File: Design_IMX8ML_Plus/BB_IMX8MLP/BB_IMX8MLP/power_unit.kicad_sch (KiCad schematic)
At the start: 0 parts

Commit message: Improve power source module in the base board
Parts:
- added C10, C12, C26, C27, C4, C7, C8: 100nF, Capacitor_SMD:C_0402_1005Metric, symbol Device:C_Small
- added C11, C14, C15, C16, C20, C5, C6: 10uF, Capacitor_SMD:C_0402_1005Metric, symbol Device:C_Small
- added C13: 1uF, Capacitor_SMD:C_0402_1005Metric, symbol Device:C_Small
- added C17, C18, C19, C21, C22, C23, C24, C3: 47uF, Capacitor_SMD:C_0402_1005Metric, symbol Device:C_Small
- added C25, C9: 4.7uF, Capacitor_SMD:C_0402_1005Metric, symbol Device:C_Small
- added D1: SS3200, Diode_SMD:D_SMA, symbol Diode:SS3200
- added F1: 10A 36R@100MHz, Fuse:Fuse_0603_1608Metric, symbol Device:Fuse_Small
- added J10: Barrel_Jack, Connector_BarrelJack:BarrelJack_CUI_PJ-063AH_Horizontal, symbol Connector:Barrel_Jack
- added L1, L2: 2.2uH_12A, Inductor_SMD:L_7.3x7.3_H3.5, symbol Device:L_Small
- added Q1, Q4: PMDT290UCE, Package_TO_SOT_SMD:SOT-666, symbol Transistor_FET:PMDT290UCE
- added Q2, Q3: NTMFS5C670NLT1G, _W_SBC:NTMFS5C670NLT1G_ONS, symbol NTMFS5C670NLT1G:NTMFS5C670NLT1G
- added R1, R19: 47K, Resistor_SMD:R_0402_1005Metric, symbol Device:R_Small
- added R10, R16, R17, R18, R21, R23, R3, R4, R5, R7, R8, R9: 100K, Resistor_SMD:R_0402_1005Metric, symbol Device:R_Small
- added R11: 787K, Resistor_SMD:R_0402_1005Metric, symbol Device:R_Small
- added R12, R14: 80.6K, Resistor_SMD:R_0402_1005Metric, symbol Device:R_Small
- added R13: 18.2K, Resistor_SMD:R_0402_1005Metric, symbol Device:R_Small
- added R15: 0.01, Resistor_SMD:R_0402_1005Metric, symbol Device:R_Small
- added R2, R20: 8.87K, Resistor_SMD:R_0402_1005Metric, symbol Device:R_Small
- added R22, R6: 510K, Resistor_SMD:R_0402_1005Metric, symbol Device:R_Small
- added SW1: Power ON/OFF, Button_Switch_SMD:SW_SPST_TL3342, symbol Switch:SW_MEC_5E
- added SW2: RESET, Button_Switch_SMD:SW_SPST_TL3342, symbol Switch:SW_MEC_5E
- added SW3: RECOVERY, Button_Switch_SMD:SW_SPST_TL3342, symbol Switch:SW_MEC_5E
- added U4: LTC4368IDD-1_PBF, Package_DFN_QFN:DFN-10-1EP_3x3mm_P0.5mm_EP1.65x2.38mm, symbol LTC4368IDD-1_PBF:LTC4368IDD-1_PBF
- added U5, U7: AOZ2261AQI-15, _W_SBC:QFN4X4-22L_EP2_S_AOS, symbol AOZ2261AQI-15:AOZ2261AQI-15
- added U6: NCV4274CST50T3G, Package_TO_SOT_SMD:SOT-223, symbol NCV4274CST50T3G:NCV4274CST50T3G
- added U8: LTC2954CDDB-1-TRMPBF, _W_SBC:DFN-8_DDB_LIT, symbol LTC2954CDDB-2:LTC2954CDDB-1-TRMPBF
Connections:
- new net: R4.1, U5.3 (*PFM)
- new net: C13.1, U8.6 (PDT)
- new net: SW1.3 (K), SW1.4 (A), U8.3 (*PB)
- new net: R7.1, U8.5 (*KILL)
- new net: R3.2, U5.1 (PGOOD)
- new net: C5.1, R14.2
- new net: R12.2, R13.1, U4.3 (OV)
- new net: C8.1, U5.22 (SS)
- new net: Q4.3 (DP), R18.1, U7.2 (EN)
- new net: C27.1, U7.22 (SS)
- new net: R21.1, U7.3 (*PFM)
- new net: R22.2, U7.6 (TON)
- new net: C7.2, L1.2, U5.10 (LX), U5.11 (LX), U5.16 (LX), U5.17 (LX), U5.18 (LX)
- new net: C7.1, U5.20 (BST)
- new net: C4.1, U4.4 (RETRY)
- new net: C6.1, D1.1 (K), F1.1, J10.1
- new net: C20.1, F1.2, Q3.5, Q3.6, R10.1, U4.1 (VIN)
- new net: Q4.5 (GP), R16.2, R17.2
- new net: Q1.5 (GP), R8.2, R9.2
- new net: Q2.4, Q3.4, R14.1, U4.10 (GATE)
- new net: R11.2, R12.1, U4.2 (UV)
- new net: R10.2, R11.1, U4.6 (~{SHDN})
- new net: Q2.5, Q2.6, R15.1, U4.8 (VOUT), U4.9 (SENSE)
- new net: R6.2, U5.6 (TON)
- new net: Q1.3 (DP), R5.1, U5.2 (EN)
- new net: R23.2, U7.1 (PGOOD)
- new net: C26.2, L2.2, U7.10 (LX), U7.11 (LX), U7.16 (LX), U7.17 (LX), U7.18 (LX)
- new net: C26.1, U7.20 (BST)
- new net: Q2.1, Q2.2, Q2.3, Q3.1, Q3.2, Q3.3
- new net: SW2.3 (K), SW2.4 (A)
- new net: SW3.3 (K), SW3.4 (A)
- new net +5V: C17.1, C18.1, C19.1, C21.1, C22.1, C23.1, C24.1, C3.1, L1.1, L2.1, R1.1, R19.1
- new net +V5_STB: C11.1, C12.1, Q1.4 (SP), Q4.4 (SP), R17.1, R7.2, R8.1, U6.3 (Q), U8.4 (VIN)
- new net +V_STB: C25.1, C9.1, R23.1, R3.1, U5.21 (VCC), U7.21 (VCC)
- new net +V_SUPPLY_FILT: C10.1, C14.1, C15.1, C16.1, R15.2, R22.1, R6.1, U5.7 (IN), U5.8 (IN), U5.9 (IN), U6.1 (I), U7.7 (IN), U7.8 (IN), U7.9 (IN)
- new net 5V_EN: R16.1, R9.1, U8.7 (EN/*EN)
- new net FB_5V: R1.2, R19.2, R2.1, R20.1, U5.5 (FB), U7.5 (FB)
- new net GND: C10.2, C11.2, C12.2, C13.2, C14.2, C15.2, C16.2, C17.2, C18.2, C19.2, C20.2, C21.2, C22.2, C23.2, C24.2, C25.2, C27.2, C3.2, C4.2, C5.2, C6.2, C8.2, C9.2, D1.2 (A), J10.2, R13.2, R18.2, R2.2, R20.2, R21.2, R4.2, R5.2, SW1.1, SW1.2, SW2.1, SW2.2, SW3.1, SW3.2, U4.11 (EXP), U4.5 (GND), U5.12 (PGND), U5.13 (PGND), U5.14 (PGND), U5.15 (PGND), U5.19 (PGND), U5.4 (AGND), U6.2 (GND), U6.4 (GND), U7.12 (PGND), U7.13 (PGND), U7.14 (PGND), U7.15 (PGND), U7.19 (PGND), U7.4 (AGND), U8.1 (GND), U8.9 (EPAD)
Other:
- company: (none) -> William Sanchez Farfan
- title: (none) -> Base board desgin

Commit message: improving the usb conector
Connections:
- net +V5_STB: now also U8.3 (*PB)
- net CTRL_ON/OFF: now reaches SW1.3 (K), SW1.4 (A)
- net CTRL_ON/OFF: no longer U8.3 (*PB)
- net CTRL_RESET: now reaches SW2.3 (K), SW2.4 (A)
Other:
- moved on the sheet: C12, C13, R7, SW1, SW2, SW3, U8

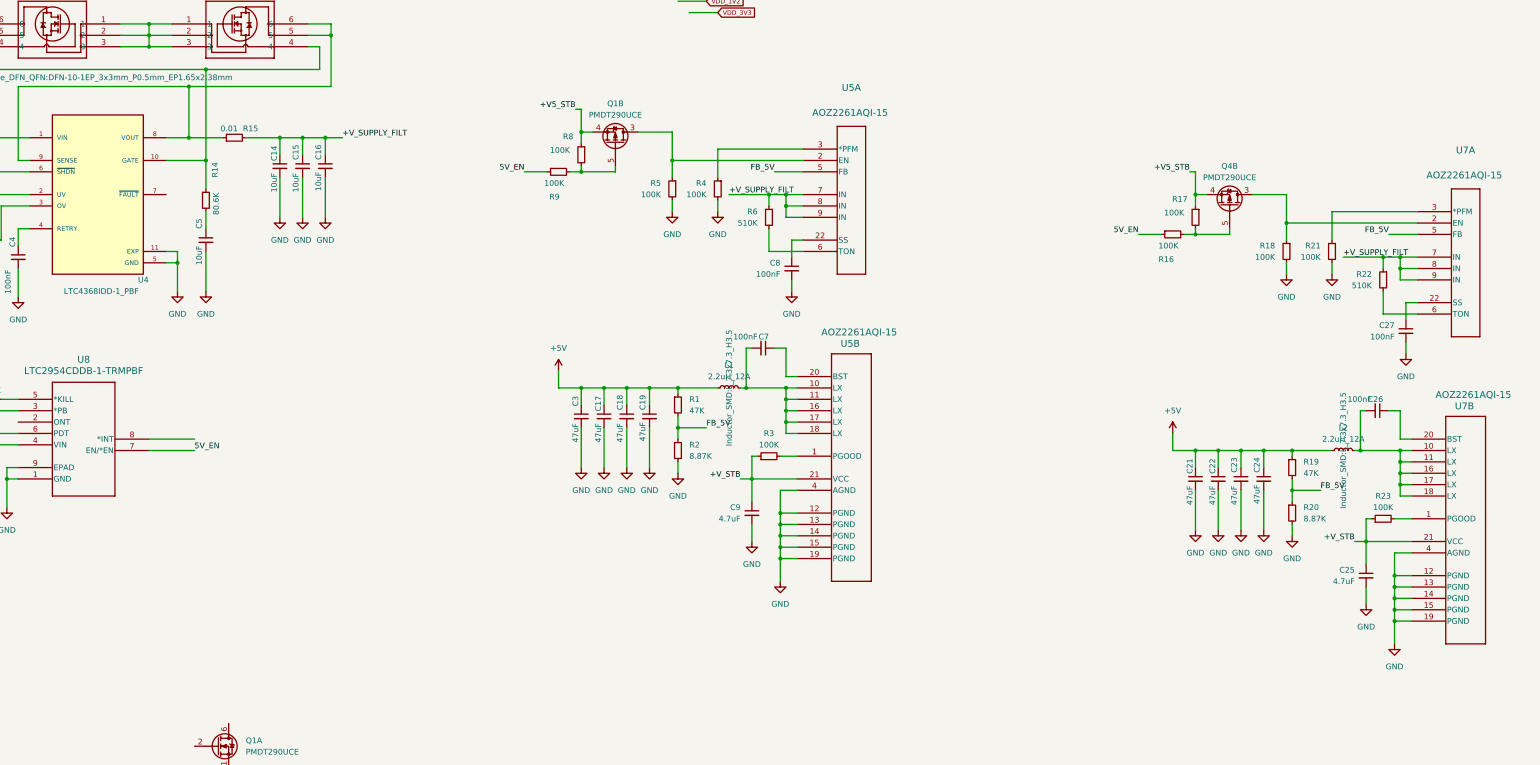
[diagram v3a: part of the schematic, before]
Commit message: improving Ethernet, USB and Camera inteface
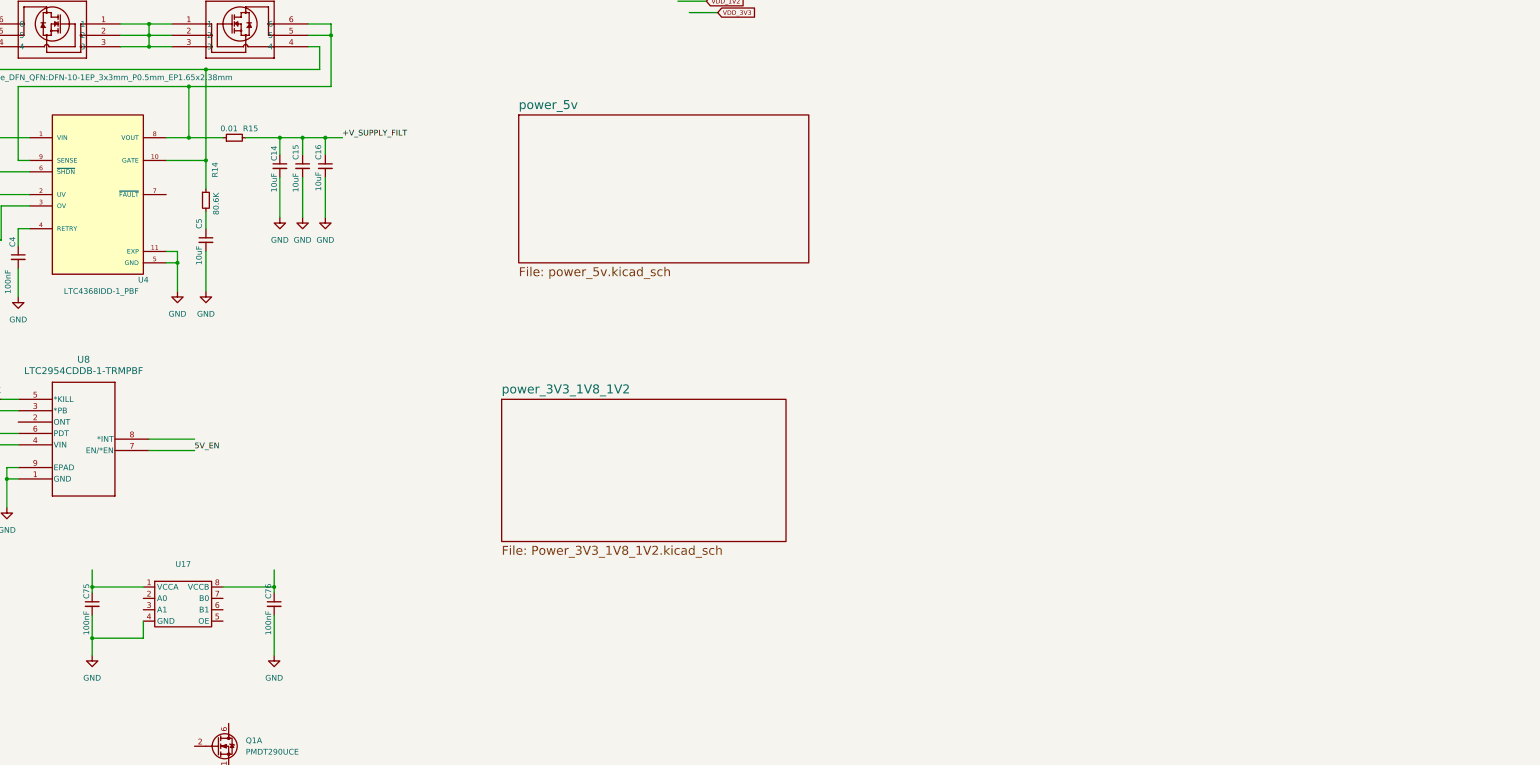
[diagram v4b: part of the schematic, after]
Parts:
- removed C17, C18, C19, C21, C22, C23, C24, C3: 47uF, Capacitor_SMD:C_0402_1005Metric, symbol Device:C_Small
- removed C25, C9: 4.7uF, Capacitor_SMD:C_0402_1005Metric, symbol Device:C_Small
- removed C26, C27, C7, C8: 100nF, Capacitor_SMD:C_0402_1005Metric, symbol Device:C_Small
- removed L1, L2: 2.2uH_12A, Inductor_SMD:L_7.3x7.3_H3.5, symbol Device:L_Small
- removed unit 2 of Q1
- removed Q4: PMDT290UCE, Package_TO_SOT_SMD:SOT-666, symbol Transistor_FET:PMDT290UCE
- removed R1, R19: 47K, Resistor_SMD:R_0402_1005Metric, symbol Device:R_Small
- removed R16, R17, R18, R21, R23, R3, R4, R5, R8, R9: 100K, Resistor_SMD:R_0402_1005Metric, symbol Device:R_Small
- removed R2, R20: 8.87K, Resistor_SMD:R_0402_1005Metric, symbol Device:R_Small
- removed R22, R6: 510K, Resistor_SMD:R_0402_1005Metric, symbol Device:R_Small
- removed U5, U7: AOZ2261AQI-15, _W_SBC:QFN4X4-22L_EP2_S_AOS, symbol AOZ2261AQI-15:AOZ2261AQI-15
- added C75, C76: 100nF, Capacitor_SMD:C_0402_1005Metric, symbol Device:C_Small
- added U17: ~, _W_SBC:MICROPAK8_1P6X1P6_ONS, symbol _W_MX8M:FXMA2102L8X
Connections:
- net GND: now also C75.2, C76.2, U17.4 (GND)
- new net: C75.1, U17.1 (VCCA)
- new net: C76.1, U17.8 (VCCB)
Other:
- added sheet power_3V3_1V8_1V2 (Power_3V3_1V8_1V2.kicad_sch)
- added sheet power_5v (power_5v.kicad_sch)

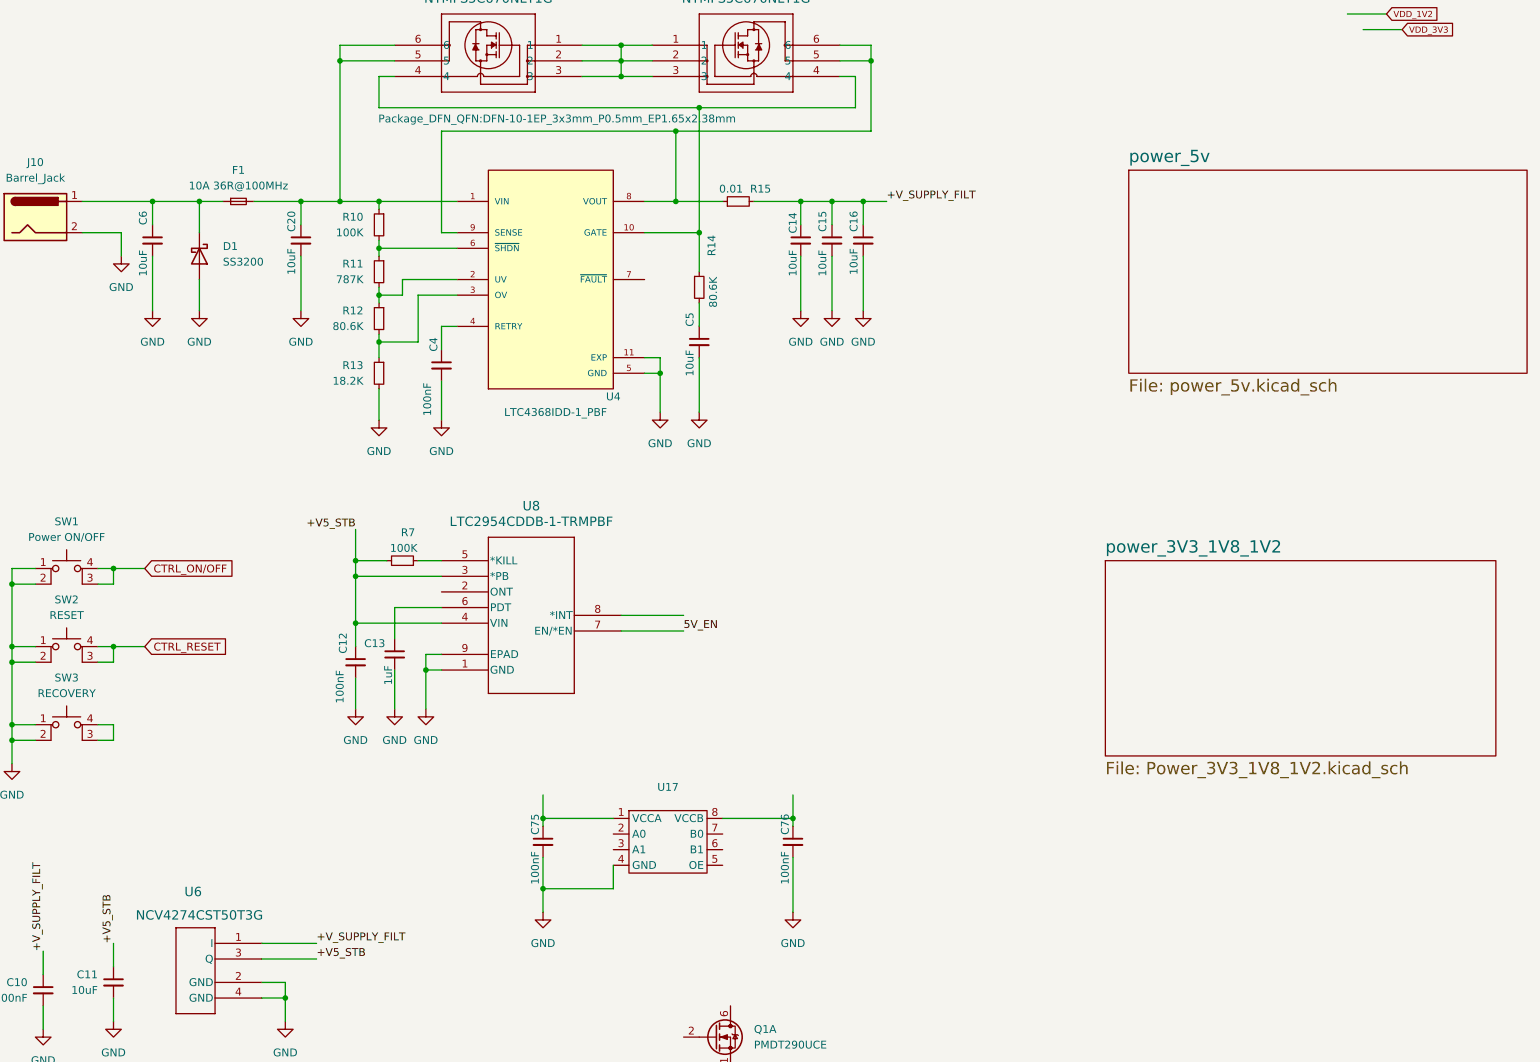
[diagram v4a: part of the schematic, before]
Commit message: Add LVDs and CSI Interface
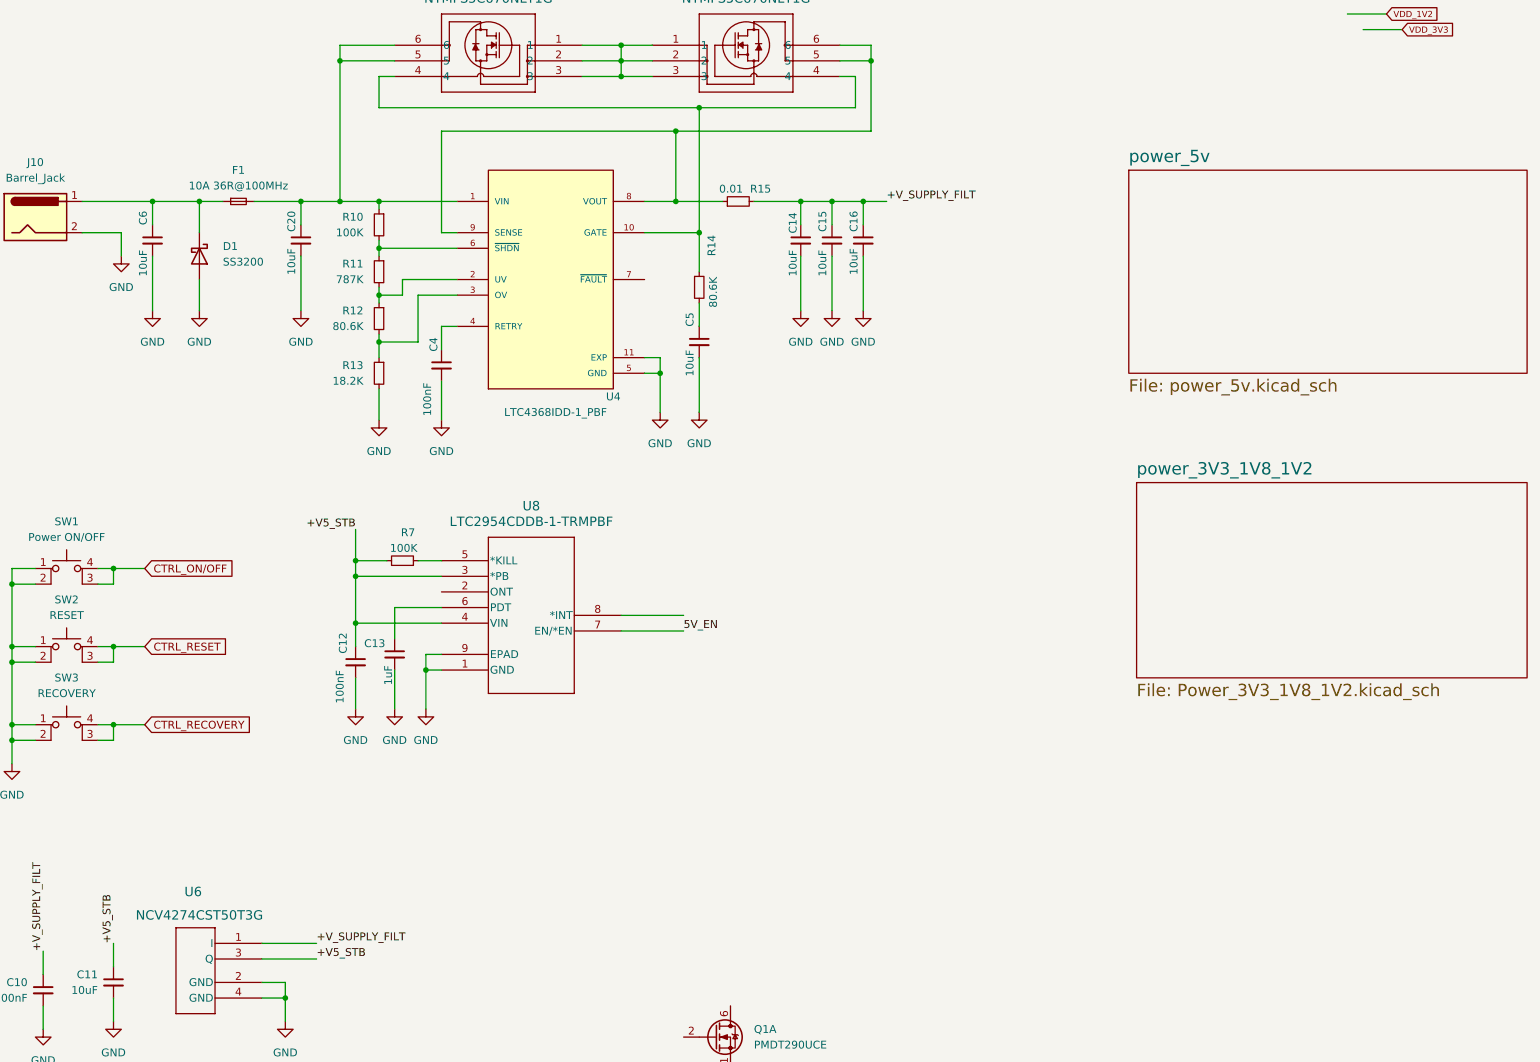
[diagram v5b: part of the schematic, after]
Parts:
- removed C75, C76: 100nF, Capacitor_SMD:C_0402_1005Metric, symbol Device:C_Small
- removed U17: ~, _W_SBC:MICROPAK8_1P6X1P6_ONS, symbol _W_MX8M:FXMA2102L8X
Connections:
- net CTRL_RECOVERY: now reaches SW3.3 (K), SW3.4 (A)

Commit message: reorganization of the componentes
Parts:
- removed Q1: PMDT290UCE, Package_TO_SOT_SMD:SOT-666, symbol Transistor_FET:PMDT290UCE
- C14, C15, C16: footprint Capacitor_SMD:C_0402_1005Metric -> Capacitor_SMD:C_1210_3225Metric_Pad1.33x2.70mm_HandSolder
- C20: footprint Capacitor_SMD:C_0402_1005Metric -> Capacitor_SMD:C_1210_3225Metric
- C5: value 10uF -> 2.2nF; footprint Capacitor_SMD:C_0402_1005Metric -> Capacitor_SMD:C_0805_2012Metric_Pad1.18x1.45mm_HandSolder
- C6: value 10uF -> 100nF
- F1: footprint Fuse:Fuse_0603_1608Metric -> Fuse:Fuse_1210_3225Metric_Pad1.42x2.65mm_HandSolder
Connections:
- net +V_SUPPLY_FILT: now also R15.1, U4.8 (VOUT); no longer R15.2
- net V_IN: now reaches C20.1, F1.2, Q3.5, Q3.6, R10.1, U4.1 (VIN)
- net at Q2.5, Q2.6, U4.9 (SENSE): now also R15.2; no longer R15.1, U4.8 (VOUT)
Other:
- moved on the sheet: C14, C15, C16, R15

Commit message: pcb reorganization
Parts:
- removed SW1: Power ON/OFF, Button_Switch_SMD:SW_SPST_TL3342, symbol Switch:SW_MEC_5E
- removed SW2: RESET, Button_Switch_SMD:SW_SPST_TL3342, symbol Switch:SW_MEC_5E
- removed SW3: RECOVERY, Button_Switch_SMD:SW_SPST_TL3342, symbol Switch:SW_MEC_5E
- added Q1: Q_NMOS_DSG, Package_TO_SOT_SMD:SOT-563, symbol Device:Q_NMOS_DSG
- added R80, R81: 100K, Resistor_SMD:R_0402_1005Metric, symbol Device:R_Small
- added SW1: ON/OFF, Button_Switch_SMD:SW_SPST_TL3342, symbol Switch:SW_Push_Dual
- added SW2: RESET, Button_Switch_SMD:SW_SPST_TL3342, symbol Switch:SW_Push_Dual
- added SW3: RECOVERY, Button_Switch_SMD:SW_SPST_TL3342, symbol Switch:SW_Push_Dual
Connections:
- net +V5_STB: now also Q1.1 (D), R80.1; no longer U8.3 (*PB)
- net 5V_EN: now also R81.2
- net CTRL_RECOVERY: now also SW3.2, SW3.4
- net CTRL_RESET: now also SW2.2, SW2.4
- net GND: now also SW1.1, SW1.3, SW2.1, SW3.1
- net CTRL_PWR_BTN: now reaches U8.8 (*INT)
- new net: Q1.3 (G), R80.2, R81.1
- new net: SW1.2, SW1.4, U8.3 (*PB)
- new net PMIC_EN_5V: Q1.2 (S)

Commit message: CPU Board actualizate
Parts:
- Q2, Q3: footprint _W_SBC:NTMFS5C670NLT1G_ONS -> NTMFS5C670NLT1G_ONS
- U4: footprint Package_DFN_QFN:DFN-10-1EP_3x3mm_P0.5mm_EP1.65x2.38mm -> LTC4368IDD-1_PBF:SON50P300X300X80-11N
- U6: footprint Package_TO_SOT_SMD:SOT-223 -> SOT-223_ONS
- U8: footprint _W_SBC:DFN-8_DDB_LIT -> DFN-8_DDB_LIT
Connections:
- net +V5_STB: no longer U8.4 (VIN)
- net 5V_EN: no longer U8.7 (EN/*EN)
- net CTRL_PWR_BTN: no longer U8.8 (*INT)
- net GND: no longer U8.1 (GND), U8.9 (EPAD)
- net at C13.1: no longer U8.6 (PDT)
- net at SW1.2, SW1.4: no longer U8.3 (*PB)
- net at U8.5 (*KILL): no longer R7.1
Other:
- moved on the sheet: U8
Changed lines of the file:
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@@
 			)
 		)
-		(property "Footprint" "_W_SBC:DFN-8_DDB_LIT"
+		(property "Footprint" "DFN-8_DDB_LIT"
 			(at 86.36 110.49 0)
 			(effects
@@
 			)
 		)
-		(property "Footprint" "Package_DFN_QFN:DFN-10-1EP_3x3mm_P0.5mm_EP1.65x2.38mm"
+		(property "Footprint" "LTC4368IDD-1_PBF:SON50P300X300X80-11N"
 			(at 105.156 39.37 0)
 			(effects
@@
 			)
 		)
-		(property "Footprint" "_W_SBC:NTMFS5C670NLT1G_ONS"
+		(property "Footprint" "NTMFS5C670NLT1G_ONS"
 			(at 109.22 26.67 0)
 			(effects
@@
 			)
 		)
-		(property "Footprint" "Package_TO_SOT_SMD:SOT-223"
+		(property "Footprint" "SOT-223_ONS"
 			(at 57.15 172.72 0)
 			(effects
@@
 			)
 		)
-		(property "Footprint" "_W_SBC:NTMFS5C670NLT1G_ONS"
+		(property "Footprint" "NTMFS5C670NLT1G_ONS"
 			(at 120.65 26.67 0)
 			(effects
